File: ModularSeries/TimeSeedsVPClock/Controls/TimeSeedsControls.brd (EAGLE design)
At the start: 48.5 x 98 mm, 19 parts

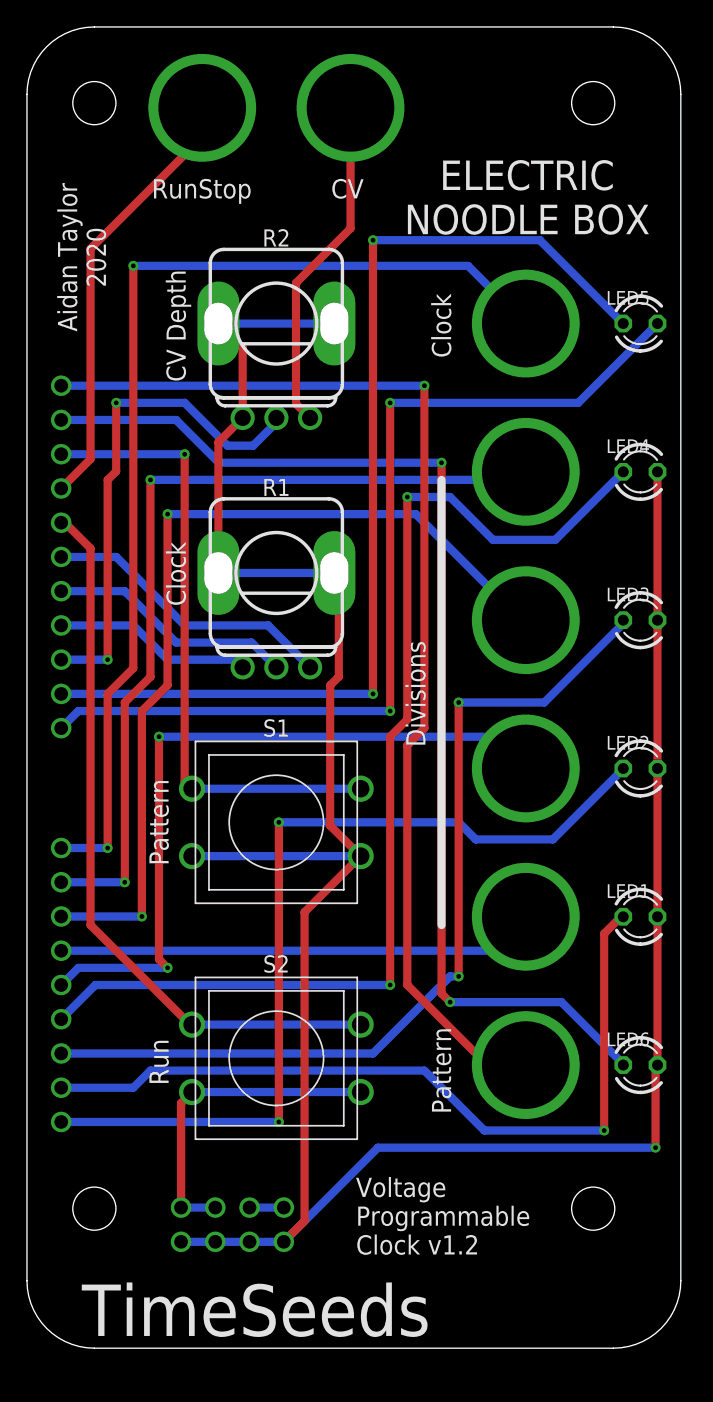
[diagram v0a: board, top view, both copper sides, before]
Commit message: Common collector + emitter follower pulse output added to Knives, docs updated
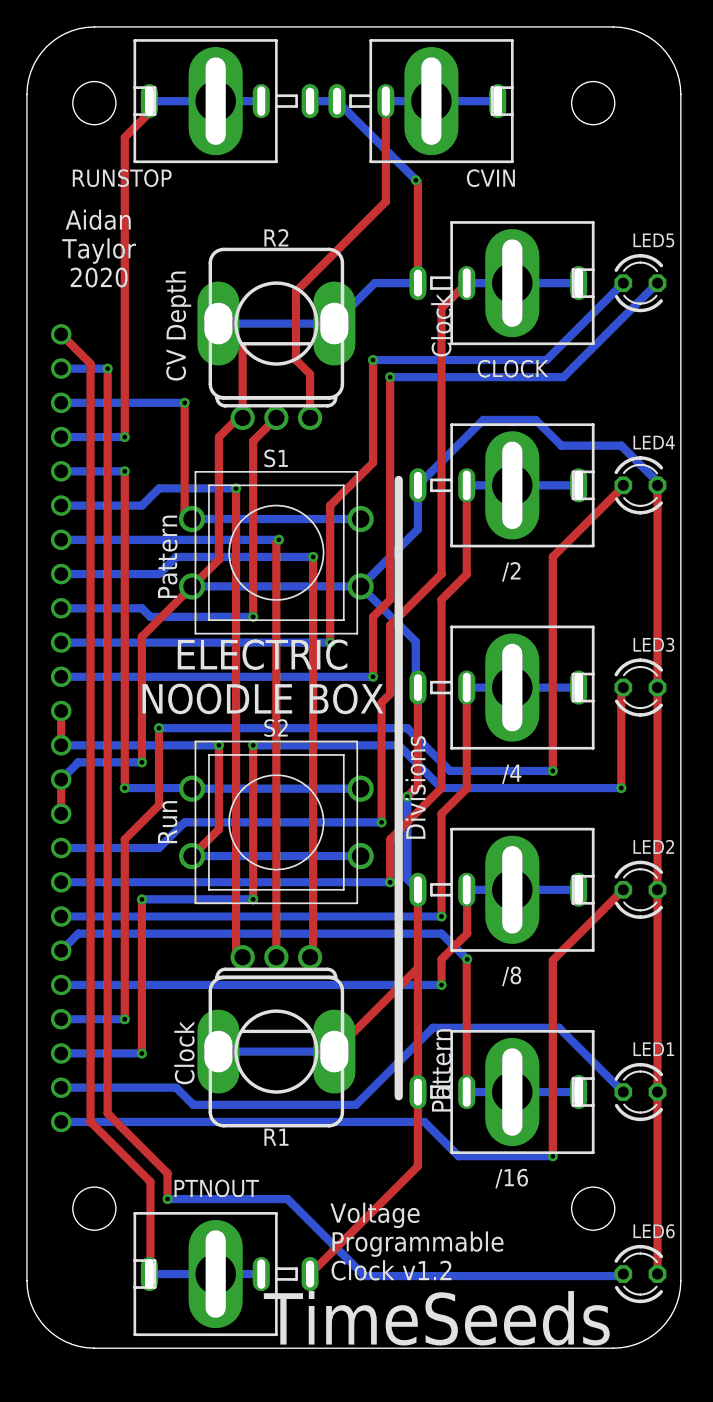
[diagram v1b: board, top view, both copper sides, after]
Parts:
- removed D16, D2, D4, D8, FREQCV: BANANA_PANEL, ElectricNoodleBox:BANANA_PANEL
- added /16, /2, /4, /8, CVIN: COMBI-JACKCINCHNANA, ElectricNoodleBox:NEWCOMBOJACK_PANEL
- CLOCK, PTNOUT, RUNSTOP: value BANANA_PANEL -> COMBI-JACKCINCHNANA; device ElectricNoodleBox:BANANA_PANEL -> ElectricNoodleBox:NEWCOMBOJACK_PANEL
- moved R1 35.5 mm to (19.5, 23.0), turned to 180 degrees
- moved PTNOUT 27.7 mm to (15.0, 6.50), turned to 90 degrees
- moved S1 20.0 mm to (19.5, 60.0)
- moved S2 17.5 mm to (19.5, 40.0)
- moved LED6 15.5 mm to (46.5, 6.50)
- moved LED1 13.0 mm to (46.5, 20.0)
- moved LED2 9.00 mm to (46.5, 35.0)
- moved LED3 5.00 mm to (46.5, 50.0)
- moved CLOCK 3.16 mm to (37.0, 80.0), turned to 270 degrees
- moved LED5 3.00 mm to (46.5, 80.0)
- moved RUNSTOP 1.12 mm to (15.0, 93.5), turned to 90 degrees
- moved LED4 1.00 mm to (46.5, 65.0)
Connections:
- removed net +5V: BOARD1.5V1, BOARD1.5V2
- net AGND: now also /16.S, /2.S, /4.S, /8.S, CLOCK.S, CVIN.S, PTNOUT.S, RUNSTOP.S; no longer BOARD1.GNDT3, BOARD1.GNDT4
- net N$16: now also CVIN.CONN, CVIN.T1, CVIN.T2; no longer FREQCV.CONN
- net N$17: now also PTNOUT.T1, PTNOUT.T2
- net N$21: now also RUNSTOP.T1, RUNSTOP.T2
- net N$5: now also /16.CONN, /16.T1, /16.T2; no longer D16.CONN
- net N$6: now also /8.CONN, /8.T1, /8.T2; no longer D8.CONN
- net N$7: now also /4.CONN, /4.T1, /4.T2; no longer D4.CONN
- net N$8: now also /2.CONN, /2.T1, /2.T2; no longer D2.CONN
- net N$9: now also CLOCK.T1, CLOCK.T2
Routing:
- net AGND: track 191.3 -> 256.0 mm, vias 1 -> 3
- net N$13: track 14.7 -> 49.0 mm, vias 0 -> 1
- net N$12: track 18.3 -> 47.2 mm, vias 0 -> 1
- net N$15: track 21.9 -> 48.5 mm, vias 0 -> 1
- net N$18: track 84.6 -> 103.1 mm
- net N$19: track 46.7 -> 30.5 mm
- net N$10: track 77.9 -> 63.1 mm
- net N$5: track 35.5 -> 49.6 mm, vias 0 -> 1
- net N$4: track 59.2 -> 46.6 mm, vias 1 -> 0
- net N$7: track 66.4 -> 54.3 mm, vias 2 -> 1
- net +12V: track 23.9 -> 35.8 mm, vias 0 -> 1
- net N$16: track 25.1 -> 35.0 mm
- net N$6: track 54.0 -> 44.4 mm, vias 2 -> 1
- net N$20: track 54.0 -> 45.7 mm, vias 0 -> 2
- net N$3: track 66.6 -> 59.4 mm, vias 2 -> 1
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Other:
- board text removed: "CV"
- board text removed: "RunStop"

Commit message: Panel for TimeSeeds added. TLHP core PCB added
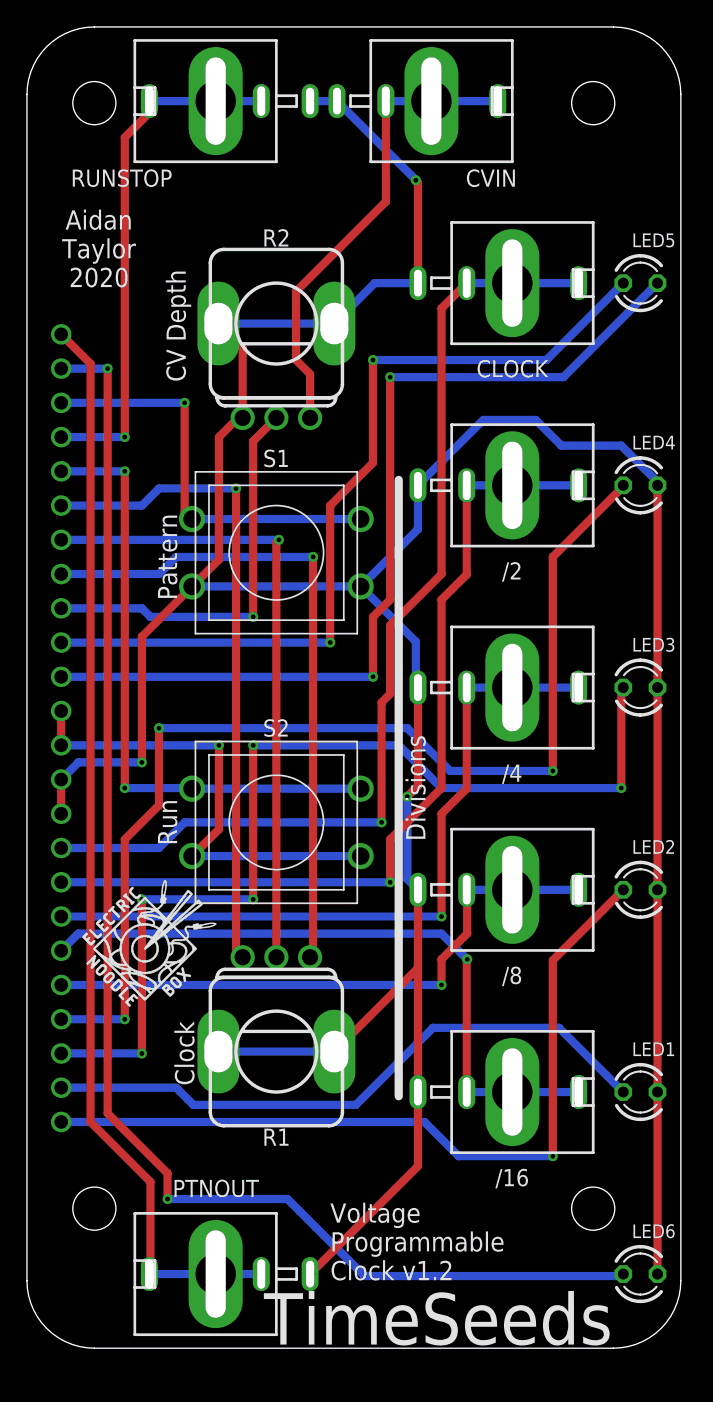
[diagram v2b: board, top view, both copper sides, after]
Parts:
- added U$1, U$2: (no value), ElectricNoodleBox:LOGO10X10
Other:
- board text removed: "ELECTRIC NOODLE BOX"
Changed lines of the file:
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@@
 <?xml version="1.0" encoding="utf-8"?>
 <!DOCTYPE eagle SYSTEM "eagle.dtd">
-<eagle version="9.6.0">
+<eagle version="9.6.2">
 <drawing>
 <settings>
@@
 <setting verticaltext="up"/>
 </settings>
-<grid distance="25" unitdist="mil" unit="mil" style="lines" multiple="1" display="no" altdistance="5" altunitdist="mil" altunit="mil"/>
+<grid distance="25" unitdist="mil" unit="mm" style="lines" multiple="1" display="no" altdistance="5" altunitdist="mil" altunit="mil"/>
 <layers>
 <layer number="1" name="Top" color="4" fill="1" visible="yes" active="yes"/>
@@
 <layer number="19" name="Unrouted" color="6" fill="1" visible="yes" active="yes"/>
 <layer number="20" name="Dimension" color="24" fill="1" visible="yes" active="yes"/>
-<layer number="21" name="tPlace" color="7" fill="1" visible="yes" active="yes"/>
+<layer number="21" name="tPlace" color="7" fill="1" visible="no" active="yes"/>
 <layer number="22" name="bPlace" color="7" fill="1" visible="yes" active="yes"/>
 <layer number="23" name="tOrigins" color="15" fill="1" visible="yes" active="yes"/>
@@
 </layers>
 <board>
+<fusionsync huburn="a.cGVyc29uYWw6dWUyYjdlNGE0" projecturn="a.cGVyc29uYWw6dWUyYjdlNGE0IzIwMjAwNDA1MjgzMzA0MTgx" f3durn="urn:adsk.wipprod:dm.lineage:TDh42G3TRJixGXYL3D15KQ" pcbguid="" lastpulledtime="" lastsyncedchangeguid="" latestrevisionid="b7a89fb4-2104-4071-8987-7635b4773628" lastsyncedrevisionid="b7a89fb4-2104-4071-8987-7635b4773628" lastboardhashguid="8a36f45e-14bc-e37d-a9bc-cc4a8f987989" lastpushedtime="2020-06-25T11:16:19Z" linktopcb3d="true"/>
 <plain>
 <wire x1="1" y1="94" x2="1" y2="6" width="0" layer="20"/>
@@
 <text x="29.845" y="42.545" size="1.4224" layer="21" font="vector" ratio="16" rot="R270" align="center">Divisions</text>
 <wire x1="28.575" y1="65.405" x2="28.575" y2="19.685" width="0.6096" layer="21"/>
-<text x="31.75" y="76.835" size="1.4224" layer="21" font="vector" ratio="16" rot="R90" align="center">Clock</text>
-<text x="31.75" y="21.59" size="1.4224" layer="21" font="vector" ratio="16" rot="R90" align="center">Pattern</text>
 <text x="23.495" y="8.89" size="1.4224" layer="21" font="vector" ratio="16" align="center-left">Voltage
 Programmable
 Clock v1.2</text>
-<text x="18.415" y="50.8" size="2.1844" layer="21" font="vector" ratio="16" align="center">ELECTRIC
-NOODLE BOX</text>
 <text x="6.35" y="82.55" size="1.4224" layer="21" font="vector" ratio="16" rot="R180" align="center">Aidan
 Taylor
@@
 <attribute name="NAME" x="37" y="73.65" size="1.27" layer="25" font="vector" align="center"/>
 </element>
+<element name="U$1" library="ElectricNoodleBox" package="LOGO10X10" value="" x="5.08" y="26.035" smashed="yes"/>
+<element name="U$2" library="ElectricNoodleBox" package="LOGO10X10" value="" x="12.7" y="79.375" smashed="yes" rot="MR0"/>
 </elements>
 <signals>
@@
 </note>
 <note version="8.3" severity="warning">
+Since Version 8.3, EAGLE supports Fusion synchronisation.
+This feature will not be available in this version and saving
+the document will break the link to the Fusion PCB feature.
+</note>
+<note version="8.3" severity="warning">

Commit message: Layout and schematic renders for LHP added
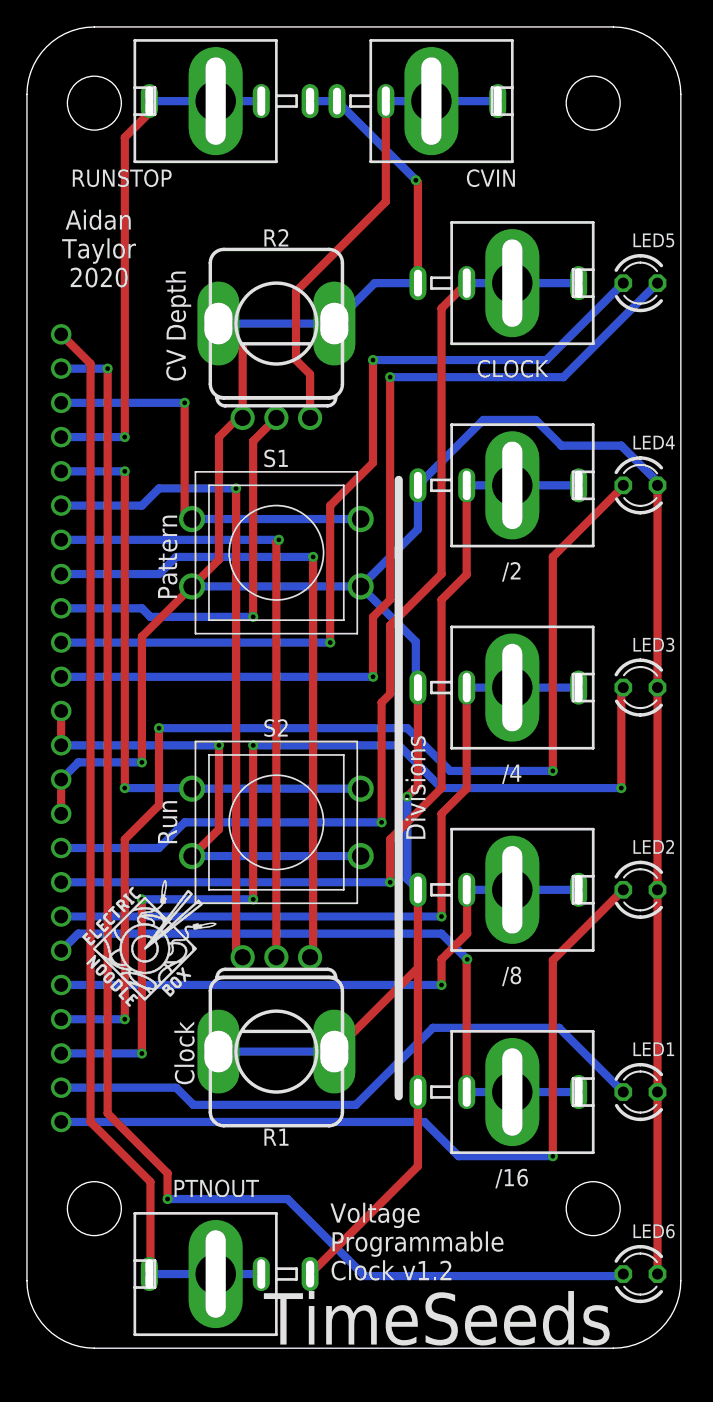
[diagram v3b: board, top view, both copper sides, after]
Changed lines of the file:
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@@
 <layer number="44" name="Drills" color="7" fill="1" visible="no" active="yes"/>
 <layer number="45" name="Holes" color="7" fill="1" visible="no" active="yes"/>
-<layer number="46" name="Milling" color="3" fill="1" visible="no" active="yes"/>
+<layer number="46" name="Milling" color="3" fill="1" visible="yes" active="yes"/>
 <layer number="47" name="Measures" color="7" fill="1" visible="no" active="yes"/>
 <layer number="48" name="Document" color="7" fill="1" visible="yes" active="yes"/>
